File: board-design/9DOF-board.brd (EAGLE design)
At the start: 100 x 80 mm, 0 parts

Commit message: Add files via upload
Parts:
- added I2C, J1, VINARDUINO: (no value), con-molex:22-23-2021
- added SERVO1, SERVO2, SERVO3, SERVO4, SERVO5, SERVO6, SERVO7, SERVO8, SERVO9: 22-23-2041, con-molex:22-23-2041
- added U$1, U$2: PRO-MINI, Arduino-clone:PRO-MINI
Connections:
- new net GND: J1.2, SERVO1.1, SERVO2.1, SERVO3.1, SERVO4.1, SERVO6.1, SERVO7.1, SERVO8.1, SERVO9.1, U$1.GND, U$1.GND2, U$1.GND3, U$2.GND, U$2.GND2, U$2.GND3, VINARDUINO.2
- new net I2C_SCL: I2C.2, U$1.A5
- new net I2C_SDA: I2C.1, U$1.A4
- new net RAW: U$1.RAW, U$2.RAW
- new net SERVO1_POT: SERVO1.4, U$1.A0
- new net SERVO1_SIG: SERVO1.3, U$1.D2
- new net SERVO2_POT: SERVO2.4, U$1.A1
- new net SERVO2_SIG: SERVO2.3, U$1.D3
- new net SERVO3_POT: SERVO3.4, U$1.A2
- new net SERVO3_SIG: SERVO3.3, U$1.D4
- new net SERVO4_POT: SERVO4.4, U$1.A3
- new net SERVO4_SIG: SERVO4.3, U$1.D5
- new net SERVO5_POT: SERVO5.4, U$1.A6
- new net SERVO5_SIG: SERVO5.3, U$1.D6
- new net SERVO6_POT: SERVO6.4, U$1.A7
- new net SERVO6_SIG: SERVO6.3, U$1.D7
- new net SERVO7_POT: SERVO7.4, U$2.A0
- new net SERVO7_SIG: SERVO7.3, U$2.D2
- new net SERVO8_POT: SERVO8.4, U$2.A1
- new net SERVO8_SIG: SERVO8.3, U$2.D3
- new net SERVO9_POT: SERVO9.4, U$2.A2
- new net SERVO9_SIG: SERVO9.3, U$2.D4
- new net VCC_ARDUINO: U$1.VCC1, U$2.VCC1, VINARDUINO.1
- new net VCC_SERVO: J1.1, SERVO1.2, SERVO2.2, SERVO3.2, SERVO4.2, SERVO5.2, SERVO6.2, SERVO7.2, SERVO8.2, SERVO9.2
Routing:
- net VCC_ARDUINO: track 0.00 -> 112.4 mm, vias 0 -> 8
- net SERVO6_POT: track 0.00 -> 95.0 mm
- net RAW: track 0.00 -> 76.7 mm, vias 0 -> 2
- net SERVO6_SIG: track 0.00 -> 67.7 mm, vias 0 -> 2
- net SERVO5_SIG: track 0.00 -> 57.2 mm, vias 0 -> 2
- net SERVO9_POT: track 0.00 -> 51.2 mm
- net SERVO5_POT: track 0.00 -> 49.6 mm
- net SERVO1_SIG: track 0.00 -> 48.4 mm, vias 0 -> 2
- net SERVO7_SIG: track 0.00 -> 48.0 mm, vias 0 -> 2
- net SERVO8_POT: track 0.00 -> 45.3 mm
- net SERVO8_SIG: track 0.00 -> 44.0 mm, vias 0 -> 2
- net SERVO7_POT: track 0.00 -> 43.9 mm
- net SERVO3_POT: track 0.00 -> 40.4 mm
- net SERVO2_POT: track 0.00 -> 40.3 mm
- net SERVO1_POT: track 0.00 -> 39.7 mm
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- added copper zone on layer 16, net GND
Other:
- board size 100 x 80 mm -> 102.5 x 74.9 mm

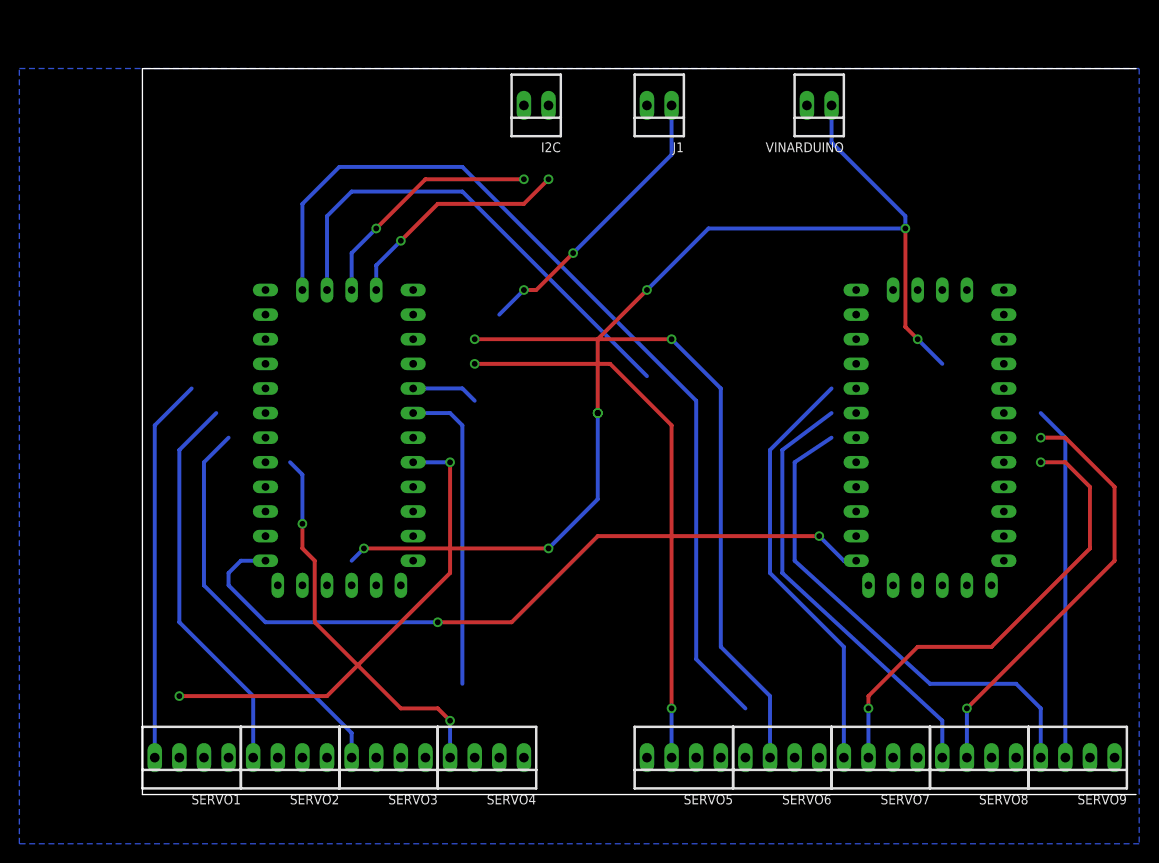
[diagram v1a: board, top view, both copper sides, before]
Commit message: SPI connections between Arduinos done
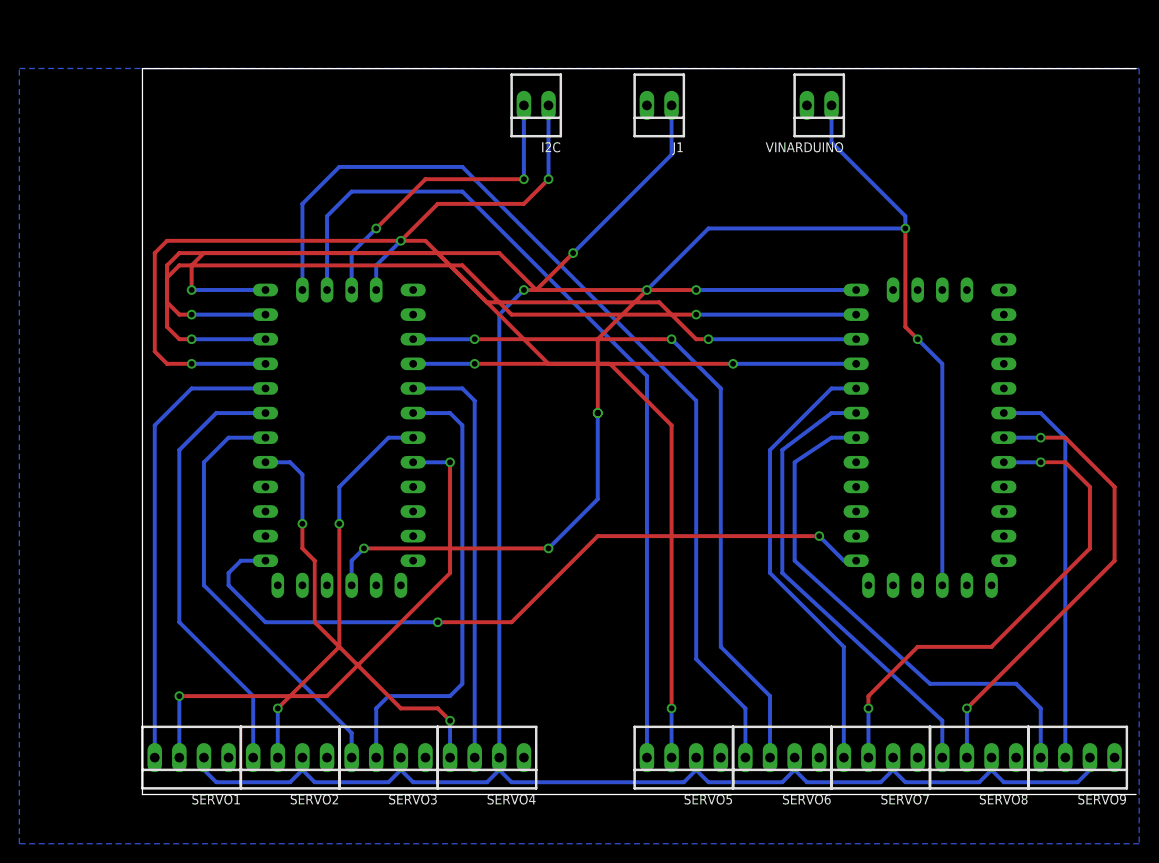
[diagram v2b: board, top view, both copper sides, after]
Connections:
- new net SPI_MISO: U$1.D12, U$2.D12
- new net SPI_MOSI: U$1.D11, U$2.D11
- new net SPI_SCLK: U$1.D13, U$2.D13
- new net SPI_SS: U$1.D10, U$2.D10
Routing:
- net VCC_SERVO: track 29.7 -> 186.7 mm
- net SPI_SCLK: track 0.00 -> 100.3 mm, vias 0 -> 2
- net SPI_MISO: track 0.00 -> 92.4 mm, vias 0 -> 2
- net SPI_MOSI: track 0.00 -> 87.0 mm, vias 0 -> 2
- net SPI_SS: track 0.00 -> 80.8 mm, vias 0 -> 2
- net SERVO2_SIG: track 0.00 -> 40.3 mm, vias 0 -> 2
- net SERVO5_POT: track 49.6 -> 89.0 mm
- net SERVO4_SIG: track 6.88 -> 43.7 mm
- net VCC_ARDUINO: track 112.4 -> 137.8 mm
- net SERVO3_SIG: track 32.3 -> 47.3 mm
- net I2C_SCL: track 24.7 -> 32.4 mm
- net I2C_SDA: track 24.0 -> 31.6 mm
- net SERVO1_POT: track 39.7 -> 47.3 mm
- net SERVO1_SIG: track 48.4 -> 54.8 mm
- net SERVO6_SIG: track 67.7 -> 74.1 mm
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
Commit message: Track size increased and jumper routings optimized.
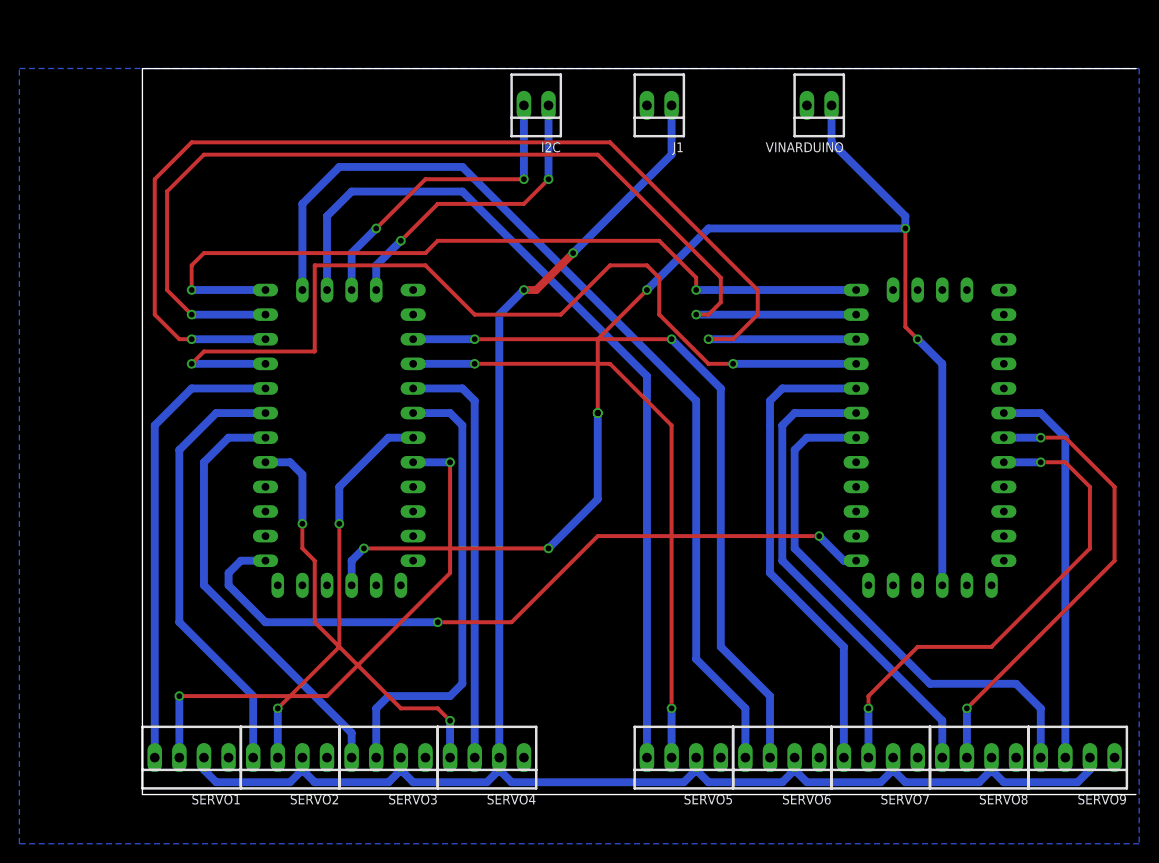
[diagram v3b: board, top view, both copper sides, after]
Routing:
- net SPI_MISO: track 92.4 -> 120.5 mm
- net SPI_MOSI: track 87.0 -> 107.5 mm
- net SPI_SCLK: track 100.3 -> 96.3 mm
- net SERVO7_POT: track 46.4 -> 49.4 mm
- net SPI_SS: track 80.8 -> 82.6 mm
- net SERVO8_POT: track 47.9 -> 49.3 mm
- net SERVO9_POT: track 53.7 -> 54.4 mm
